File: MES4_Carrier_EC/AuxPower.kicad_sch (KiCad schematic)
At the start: 45 parts, among them J14 IMU 9V, J15 SERVO 24V, J16 SCREEN 5V, J17 SERVO UART, SW2 SS12D10G5, U10 URB2405YMD-20WR3, U9 URB2409S-10WR3

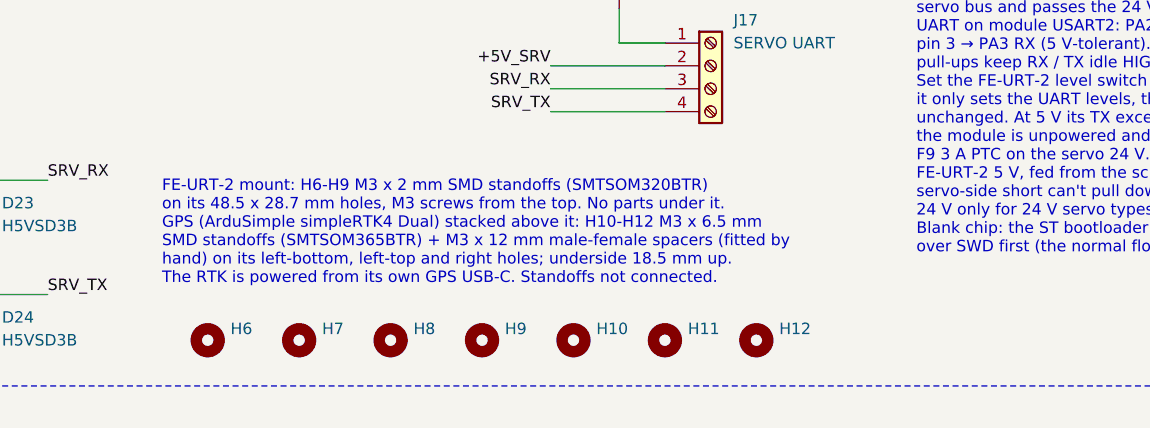
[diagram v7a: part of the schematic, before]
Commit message: Place every part, tidy the converter block, leave out the GPS mount
- Converter block: U1/U9/U10 right-aligned in one line beside the
  FE-URT-2 (2.5 mm channel), all their caps on the left in routing lanes.
- STDC14 (J2) and RESET above the M.2 connector, ESD diodes beside J1;
  ADS1232 load-cell front end below the MES4-MCU; sensor optos below the
  converter block.
- Supply LEDs (24V/9V/5V/3V3) in one array with knockout voltages, as on
  the Flasher; pull-ups beside it.
- Terminal label boxes on the FE-URT-2 connectors J17/J15 (moved up 2 mm).
- GPS (simpleRTK4) mount left out for now: GPS_MOUNT = False in gen.py
  drops H_GPS1-3; A2 and the standoffs are off the PCB.
- Top-row reshuffle, relay channels in a column, FE-URT-2 portrait.

DRC: 11 silkscreen warnings (edge clearance, J1 circle), schematic parity clean.

Co-Authored-By: Claude Opus 5.5 <noreply@anthropic.com>
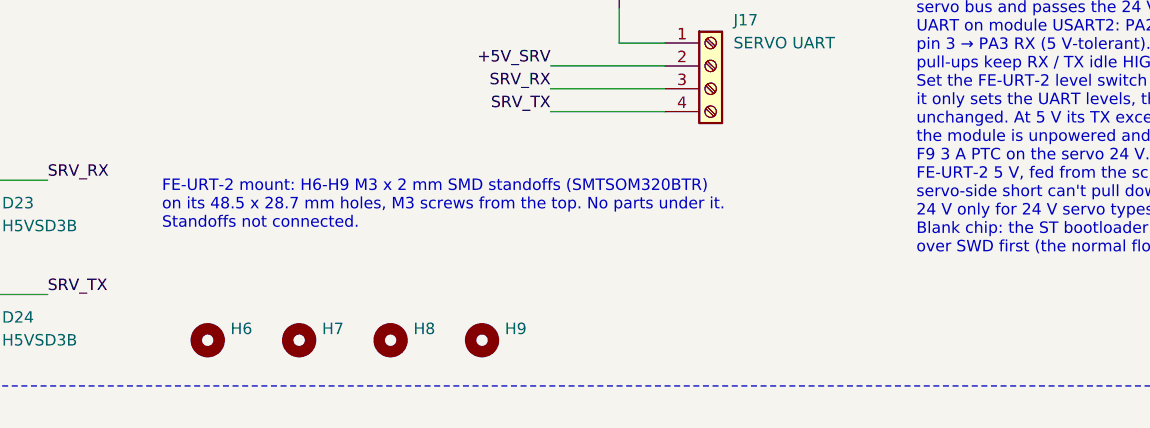
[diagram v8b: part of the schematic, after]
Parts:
- removed H10, H11, H12: M3 standoff 6.5mm, MES4-Carrier-EC:Standoff_SMD_M3_H6.5mm_SMTSOM365BTR, symbol Mechanical:MountingHole
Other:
- note added: "FE-URT-2 mount: H6-H9 M3 x 2 mm SMD standoffs (SMTSOM320BTR) on its 48.5 x 28.7 mm holes, M3 screws from the top. No parts under it. Standoffs not connected."
- note removed: "FE-URT-2 mount: H6-H9 M3 x 2 mm SMD standoffs (SMTSOM320BTR) on its 48.5 x 28.7 mm holes, M3 screws from the top. No parts under it. GPS (ArduSimple simpleRTK4 Dual) stacked above it: H10-H12 M3 x 6.5 mm SMD standoffs (SMTSOM365BTR) + M3 x 12 mm male-female spacers (fitted by hand) on its left-bottom, left-top and right holes; underside 18.5 mm up. The RTK is powered from its own GPS USB-C. Stand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"
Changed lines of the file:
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@@
 		(effects (font (size 1.27 1.27)) (justify left top))
 	)
-	(text "FE-URT-2 mount: H6-H9 M3 x 2 mm SMD standoffs (SMTSOM320BTR)\non its 48.5 x 28.7 mm holes, M3 screws from the top. No parts under it.\nGPS (ArduSimple simpleRTK4 Dual) stacked above it: H10-H12 M3 x 6.5 mm\nSMD standoffs (SMTSOM365BTR) + M3 x 12 mm male-female spacers (fitted by\nhand) on its left-bottom, left-top and right holes; underside 18.5 mm up.\nThe RTK is powered from its own GPS USB-C. Standoffs not connected."
+	(text "FE-URT-2 mount: H6-H9 M3 x 2 mm SMD standoffs (SMTSOM320BTR)\non its 48.5 x 28.7 mm holes, M3 screws from the top. No parts under it.\nStandoffs not connected."
 		(exclude_from_sim no)
 		(at 210.82 226.06 0)
@@
 					(unit 1)
 				)
-			)
-		)
-	)
-	(symbol
-		(lib_id "Mechanical:MountingHole")
-		(at 256.54 243.84 0)
-		(unit 1)
-		(exclude_from_sim no)
-		(in_bom yes)
-		(on_board yes)
-		(dnp no)
-		(property "Reference" "H10"
-			(at 259.08 242.57 0)
-			(effects (font (size 1.27 1.27)) (justify left))
-		)
-		(property "Value" "M3 standoff 6.5mm"
-			(at 259.08 245.11 0)
-			(effects (font (size 1.27 1.27)) (justify left) (hide yes))
-		)
-		(property "Footprint" "MES4-Carrier-EC:Standoff_SMD_M3_H6.5mm_SMTSOM365BTR"
-			(at 256.54 243.84 0)
-			(effects (font (size 1.27 1.27)) (hide yes))
-		)
-		(property "Datasheet" "~"
-			(at 256.54 243.84 0)
-			(effects (font (size 1.27 1.27)) (hide yes))
-		)
-		(property "Description" "GPS mount: M3 x 6.5 mm SMD standoff (YIYUAN SMTSOM365BTR) + M3 x 12 mm male-female spacer, not connected"
-			(at 256.54 243.84 0)
-			(effects (font (size 1.27 1.27)) (hide yes))
-		)
-		(property "LCSC" "C5301796"
-			(at 256.54 243.84 0)
-			(effects (font (size 1.27 1.27)) (hide yes))
-		)
-		(instances
-			(project "MES4_Carrier_EC"
-				(path "/0d8fbf0e-dd62-5be6-8889-307c6423adb0/564e9a93-7402-5291-998d-8aa4e1f40b1f"
-					(reference "H10")
-					(unit 1)
-				)
-			)
-		)
-	)
-	(symbol
-		(lib_id "Mechanical:MountingHole")
-		(at 266.7 243.84 0)
-		(unit 1)
-		(exclude_from_sim no)
-		(in_bom yes)
-		(on_board yes)
-		(dnp no)
-		(property "Reference" "H11"
-			(at 269.24 242.57 0)
-			(effects (font (size 1.27 1.27)) (justify left))
-		)
-		(property "Value" "M3 standoff 6.5mm"
-			(at 269.24 245.11 0)
-			(effects (font (size 1.27 1.27)) (justify left) (hide yes))
-		)
-		(property "Footprint" "MES4-Carrier-EC:Standoff_SMD_M3_H6.5mm_SMTSOM365BTR"
-			(at 266.7 243.84 0)
-			(effects (font (size 1.27 1.27)) (hide yes))
-		)
-		(property "Datasheet" "~"
-			(at 266.7 243.84 0)
-			(effects (font (size 1.27 1.27)) (hide yes))
-		)
-		(property "Description" "GPS mount: M3 x 6.5 mm SMD standoff (YIYUAN SMTSOM365BTR) + M3 x 12 mm male-female spacer, not connected"
-			(at 266.7 243.84 0)
-			(effects (font (size 1.27 1.27)) (hide yes))
-		)
-		(property "LCSC" "C5301796"
-			(at 266.7 243.84 0)
-			(effects (font (size 1.27 1.27)) (hide yes))
-		)
-		(instances
-			(project "MES4_Carrier_EC"
-				(path "/0d8fbf0e-dd62-5be6-8889-307c6423adb0/564e9a93-7402-5291-998d-8aa4e1f40b1f"
-					(reference "H11")
-					(unit 1)
-				)
-			)
-		)
-	)
-	(symbol
-		(lib_id "Mechanical:MountingHole")
-		(at 276.86 243.84 0)
-		(unit 1)
-		(exclude_from_sim no)
-		(in_bom yes)
-		(on_board yes)
-		(dnp no)
-		(property "Reference" "H12"
-			(at 279.4 242.57 0)
-			(effects (font (size 1.27 1.27)) (justify left))
-		)
-		(property "Value" "M3 standoff 6.5mm"
-			(at 279.4 245.11 0)
-			(effects (font (size 1.27 1.27)) (justify left) (hide yes))
-		)
-		(property "Footprint" "MES4-Carrier-EC:Standoff_SMD_M3_H6.5mm_SMTSOM365BTR"
-			(at 276.86 243.84 0)
-			(effects (font (size 1.27 1.27)) (hide yes))
-		)
-		(property "Datasheet" "~"
-			(at 276.86 243.84 0)
-			(effects (font (size 1.27 1.27)) (hide yes))
-		)
-		(property "Description" "GPS mount: M3 x 6.5 mm SMD standoff (YIYUAN SMTSOM365BTR) + M3 x 12 mm male-female spacer, not connected"
-			(at 276.86 243.84 0)
-			(effects (font (size 1.27 1.27)) (hide yes))
-		)
-		(property "LCSC" "C5301796"
-			(at 276.86 243.84 0)
-			(effects (font (size 1.27 1.27)) (hide yes))
-		)
-		(instances
-			(project "MES4_Carrier_EC"
-				(path "/0d8fbf0e-dd62-5be6-8889-307c6423adb0/564e9a93-7402-5291-998d-8aa4e1f40b1f"
-					(reference "H12")
-					(unit 1)
-				)
